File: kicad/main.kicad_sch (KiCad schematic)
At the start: 63 parts, among them J1 Jack-DC, J10 RS232, J11 UART, J2 LCD_Conn, J3 Data, J4 PWR, J5 uSD, J6 VIA_B, J7 IO~{EN}_{[2..7]}, J8 Control, J9 Addr, P1 Mini-DIN-6, SW1 Step, SW2 Reset, U1 74HC00, U2 74HC00, U3 MAX232, X1 4 MHz, X2 1.8432 MHz

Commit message: Add RTC & CR2032 battery, increase size of decoupling capacitors
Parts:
- removed J6: VIA_B, Connector_PinHeader_2.54mm:PinHeader_1x08_P2.54mm_Vertical, symbol Connector:Conn_01x08_Pin
- added BT1: CR2032, my:BatteryHolder_CR2032, symbol Device:Battery_Cell
- added J12: I2C1, Connector_PinHeader_2.54mm:PinHeader_1x04_P2.54mm_Horizontal, symbol Connector:Conn_01x04_Pin
- added J13: I2C2, Connector_PinHeader_2.54mm:PinHeader_2x02_P2.54mm_Vertical, symbol Connector:Conn_01x04_Pin
- added J6: VIA_B, Connector_PinHeader_2.54mm:PinHeader_1x04_P2.54mm_Vertical, symbol Connector:Conn_01x04_Pin
- added R10, R11: 5K, Resistor_THT:R_Axial_DIN0204_L3.6mm_D1.6mm_P7.62mm_Horizontal, symbol Device:R
- added U4: DS1307N+, Package_DIP:DIP-8_W7.62mm, symbol Timer_RTC:DS1307N+
- added U5: MCP9808_MSOP, Package_SO:MSOP-8_3x3mm_P0.65mm, symbol Sensor_Temperature:MCP9808_MSOP
- added Y1: 32.768 KHz, Crystal:Crystal_C26-LF_D2.1mm_L6.5mm_Horizontal, symbol Device:Crystal
- C11, C3, C4, C5, C7, C8: footprint Capacitor_THT:C_Disc_D3.0mm_W2.0mm_P2.50mm -> Capacitor_THT:C_Rect_L13.0mm_W3.0mm_P10.00mm_FKS3_FKP3_MKS4
- C16, C2, C6, C9: footprint Capacitor_THT:C_Disc_D3.0mm_W2.0mm_P2.50mm -> Capacitor_THT:C_Rect_L18.0mm_W5.0mm_P15.00mm_FKS3_FKP3
- R8, R9: footprint Resistor_THT:R_Axial_DIN0204_L3.6mm_D1.6mm_P2.54mm_Vertical -> Resistor_THT:R_Axial_DIN0204_L3.6mm_D1.6mm_P7.62mm_Horizontal
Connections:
- net +5V: now also J12.2 (Pin_2), J13.2 (Pin_2), J6.2 (Pin_2), R10.2, R11.2, U4.8 (VCC), U5.8 (V_{DD})
- net GND: now also BT1.2 (-), J12.1 (Pin_1), J13.1 (Pin_1), J6.1 (Pin_1), U4.4 (GND), U5.4 (GND), U5.5 (A2), U5.6 (A1), U5.7 (A0)
- net I^{2}CDATA: now reaches VIA1.15 (PB5)
- net I^{2}CDATA: now also J12.4 (Pin_4), J13.4 (Pin_4), R10.1, U4.5 (SDA), U5.1 (SDA)
- net I^{2}CCLK: now reaches VIA1.16 (PB6)
- net I^{2}CCLK: now also J12.3 (Pin_3), J13.3 (Pin_3), R11.1, U4.6 (SCL), U5.2 (SCL)
- net at VIA1.17 (PB7): now also J6.3 (Pin_3)
- net at VIA1.18 (CB1): now also J6.4 (Pin_4)
- new net: BT1.1 (+), U4.3 (VBAT)
- new net: U4.1 (X1), Y1.1
- new net: U4.2 (X2), Y1.2
- no-connect marks 21 -> 23
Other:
- note added: "8 256B blocks (C000-C7FF)"
- note added: "RTC"
- note added: "Temperature"
- note removed: "8 256-byte IO blocks (C000-C7FF)"
- moved on the sheet: C1, C11, C2, C3, C4, C5, C6, C7, C8, C9, CPU1, D1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

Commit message: WIP: V16
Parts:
- removed C11, C4: 0,1uF, Capacitor_THT:C_Rect_L13.0mm_W3.0mm_P10.00mm_FKS3_FKP3_MKS4, symbol Device:C
- removed C12, C13, C14, C15: 10uF, Capacitor_THT:CP_Radial_D5.0mm_P2.50mm, symbol Device:C_Polarized
- removed C5, C7: 0.1uF, Capacitor_THT:C_Rect_L13.0mm_W3.0mm_P10.00mm_FKS3_FKP3_MKS4, symbol Device:C
- removed J10: RS232, Connector_Dsub:DSUB-9_Male_Horizontal_P2.77x2.84mm_EdgePinOffset4.94mm_Housed_MountingHolesOffset7.48mm, symbol Connector:DE9_Plug
- removed J11: UART, Connector_PinHeader_2.54mm:PinHeader_1x04_P2.54mm_Horizontal, symbol Connector:Conn_01x04_Pin
- removed J13: I2C2, Connector_PinHeader_2.54mm:PinHeader_2x02_P2.54mm_Vertical, symbol Connector:Conn_01x04_Pin
- removed J2: LCD_Conn, my:LCD_4004, symbol Connector:Conn_01x18_Socket
- removed J7: IO~{EN}_{[2..7]}, Connector_PinHeader_2.54mm:PinHeader_1x06_P2.54mm_Vertical, symbol Connector:Conn_01x06_Pin
- removed JP1: Clock_Mode, Connector_PinHeader_2.54mm:PinHeader_1x03_P2.54mm_Vertical, symbol Jumper:Jumper_3_Open
- removed JP2: ACIA~{IRQ}, Connector_PinHeader_2.54mm:PinHeader_1x02_P2.54mm_Vertical, symbol Jumper:Jumper_2_Open
- removed JP3: ACIA~{NMI}, Connector_PinHeader_2.54mm:PinHeader_1x02_P2.54mm_Vertical, symbol Jumper:Jumper_2_Open
- removed JP4: VIA~{IRQ}, Connector_PinHeader_2.54mm:PinHeader_1x02_P2.54mm_Vertical, symbol Jumper:Jumper_2_Open
- removed JP5: VIA~{NMI}, Connector_PinHeader_2.54mm:PinHeader_1x02_P2.54mm_Vertical, symbol Jumper:Jumper_2_Open
- removed JP6: ~{CTS}, Connector_PinHeader_2.54mm:PinHeader_1x02_P2.54mm_Vertical, symbol Jumper:Jumper_2_Open
- removed STEP1: DS1813, Package_TO_SOT_THT:TO-92, symbol ds1813:DS1813-5+
- removed SW1: Step, Button_Switch_THT:SW_PUSH_6mm_H5mm, symbol Switch:SW_Push
- removed U3: MAX232, Package_DIP:DIP-16_W7.62mm_Socket, symbol Interface_UART:MAX232
- added C10: 10uF, Capacitor_THT:C_Disc_D3.0mm_W2.0mm_P2.50mm, symbol Device:C
- added C12: 22uF, Capacitor_THT:C_Disc_D3.0mm_W2.0mm_P2.50mm, symbol Device:C
- added C13: 0.1uF, Capacitor_THT:C_Rect_L18.0mm_W5.0mm_P15.00mm_FKS3_FKP3, symbol Device:C
- added D3: DATA, LED_THT:LED_D3.0mm, symbol Device:LED
- added J14: LCD_Conn, my:LCD24064, symbol Connector:Conn_01x22_Socket
- added J15: VIA_A, Connector_PinHeader_2.54mm:PinHeader_2x06_P2.54mm_Vertical, symbol Connector:Conn_01x12_Pin
- added J2: UART, Connector_PinHeader_2.54mm:PinHeader_1x04_P2.54mm_Horizontal, symbol Connector:Conn_01x04_Pin
- added J7: IO~{EN}_{[3..7]}, Connector_PinHeader_2.54mm:PinHeader_1x05_P2.54mm_Vertical, symbol Connector:Conn_01x05_Pin
- added MH3: MountingHole, my:Hole_3.5x5, symbol Custom_Symbols_Library:MountingHole
- added R12: 300, Resistor_THT:R_Axial_DIN0204_L3.6mm_D1.6mm_P7.62mm_Horizontal, symbol Device:R
- added R13, R14, R15: 10K, Resistor_THT:R_Axial_DIN0204_L3.6mm_D1.6mm_P7.62mm_Horizontal, symbol Device:R
- added SW3: SW_PWR, my:PB22E06, symbol Switch:SW_DPST
- added U3: AMS1117, Package_TO_SOT_SMD:SOT-223-3_TabPin2, symbol Regulator_Linear:AMS1117
- added U6: GAL16V8, Package_DIP:DIP-20_W7.62mm_Socket, symbol Logic_Programmable:GAL16V8
- added U7: ESP-01, my:ESP-01, symbol my:ESP-01
- J12: footprint Connector_PinHeader_2.54mm:PinHeader_1x04_P2.54mm_Horizontal -> Connector_PinHeader_2.54mm:PinHeader_2x02_P2.54mm_Vertical
- R8, R9: footprint Resistor_THT:R_Axial_DIN0204_L3.6mm_D1.6mm_P7.62mm_Horizontal -> Resistor_THT:R_Axial_DIN0204_L3.6mm_D1.6mm_P2.54mm_Vertical
- X1: value 4 MHz -> 16 MHz
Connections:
- net +5V: now also RV1.1, C10.1, C13.1, J14.19 (Pin_19), J14.21 (Pin_21), J14.3 (Pin_3), J15.2 (Pin_2), J2.2 (Pin_2), U3.3 (VI), U6.20 (VCC); no longer RV1.3
- net +9V: now also SW3.4; no longer J1.1
- net A_{0}: now also J14.8 (Pin_8)
- net D_{0}: now also J14.11 (Pin_11)
- net D_{1}: now also J14.12 (Pin_12)
- net D_{2}: now also J14.13 (Pin_13)
- net D_{3}: now also J14.14 (Pin_14)
- net D_{4}: now also J14.15 (Pin_15)
- net D_{5}: now also J14.16 (Pin_16)
- net D_{6}: now also J14.17 (Pin_17)
- net D_{7}: now also J14.18 (Pin_18)
- net GND: now also ACIA1.9 (~{CTS}), C10.2, C12.2, C13.2, D3.1 (K), J14.2 (Pin_2), J14.22 (Pin_22), J15.1 (Pin_1), J2.1 (Pin_1), SW3.2, U3.1 (ADJ), U6.10 (GND), U6.11 (I10/~{OE}), U7.4 (GND); no longer J1.2, RV1.1
- net IO~{EN}_{3}: now also J7.1 (Pin_1)
- net IO~{EN}_{4}: now also J7.2 (Pin_2)
- net IO~{EN}_{5}: now also J7.3 (Pin_3)
- net IO~{EN}_{6}: now also J7.4 (Pin_4)
- net IO~{EN}_{7}: now also J7.5 (Pin_5)
- net ~{IRQ}: now also ACIA1.26 (~{IRQ}), VIA1.21 (~{IRQ})
- net ~{RD}: now also J14.6 (Pin_6)
- net ~{WD}: now also J14.5 (Pin_5)
- net Ф2: now also U6.13 (IO7); no longer CPU1.37 (ϕ0)
- net TX: now reaches ACIA1.10 (TxD)
- net TX: now also J2.3 (Pin_3), U7.1 (RX)
- net RX: now reaches ACIA1.12 (RxD)
- net RX: now also J2.4 (Pin_4), U7.5 (TX)
- net at RV1.2: now also J14.4 (Pin_4)
- net at VIA1.39 (CA2): now also J15.12 (Pin_12)
- net at VIA1.40 (CA1): now also J15.11 (Pin_11)
- net CLK: no longer names the net of X1.8 (OUT)
- net CLK: now also U6.1 (I1/CLK)
- net IO~{EN}_{2} renamed LCD~{EN}
- net LCD~{EN}: now also J14.7 (Pin_7), U6.2 (I2)
- net LCDD4: no longer names the net of VIA1.2 (PA0)
- net LCDD4: now also J15.3 (Pin_3)
- net LCDD5: no longer names the net of VIA1.3 (PA1)
- net LCDD5: now also J15.4 (Pin_4)
- net LCDD6: no longer names the net of VIA1.4 (PA2)
- net LCDD6: now also J15.5 (Pin_5)
- net LCDD7: no longer names the net of VIA1.5 (PA3)
- net LCDD7: now also J15.6 (Pin_6)
- net LCDEN1: no longer names the net of VIA1.6 (PA4)
- net LCDEN1: now also J15.7 (Pin_7)
- net LCDEN2: no longer names the net of VIA1.7 (PA5)
- net LCDEN2: now also J15.8 (Pin_8)
- net LCDRS: no longer names the net of VIA1.9 (PA7)
- net LCDRS: now also J15.10 (Pin_10)
- net LCDR~{W}: no longer names the net of VIA1.8 (PA6)
- net LCDR~{W}: now also J15.9 (Pin_9)
- new net: J1.1, SW3.3
- new net: J1.2, SW3.1
- new net: R14.1, U7.7 (~{RST})
- new net: D3.2 (A), R12.1
- new net: J14.20 (Pin_20), RV1.3
- new net: R13.1, U7.2 (GPIO0)
- new net: R12.2, U7.3 (GPIO2)
- new net: R15.1, U7.6 (CH_EN)
- new net +3.3V: C12.1, R13.2, R14.2, R15.2, U3.2 (VO), U7.8 (VCC)
- new net PHV: CPU1.37 (ϕ0), U6.12 (IO8)
- no-connect marks 23 -> 33
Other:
- note added: "$D200-$D2FF"
- note added: "24064 LCD Connector"
- note added: "Modem"
- note removed: "40x04 LCD Connector"
- moved on the sheet: ACIA1, BT1, C1, C16, C2, C3, C6, C8, C9, CPU1, D1, D2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

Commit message: WIP: V16 GAL stuff
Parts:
- removed J6: VIA_B, Connector_PinHeader_2.54mm:PinHeader_1x04_P2.54mm_Vertical, symbol Connector:Conn_01x04_Pin
- removed J7: IO~{EN}_{[3..7]}, Connector_PinHeader_2.54mm:PinHeader_1x05_P2.54mm_Vertical, symbol Connector:Conn_01x05_Pin
- added J7: IO~{EN}_{[3..4]}, Connector_PinHeader_2.54mm:PinHeader_1x02_P2.54mm_Vertical, symbol Connector:Conn_01x02_Pin
- J2: footprint Connector_PinHeader_2.54mm:PinHeader_1x04_P2.54mm_Horizontal -> Connector_PinHeader_2.54mm:PinHeader_1x04_P2.54mm_Vertical
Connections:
- net IO~{EN}_{3}: now also J7.1 (Pin_1)
- net IO~{EN}_{4}: now also J7.2 (Pin_2)
- net ~{RES}: now also U6.9 (I9)
- net IO~{EN}_{5}: no longer names the net of IO1.10 (O5)
- net IO~{EN}_{6}: no longer names the net of IO1.9 (O6)
- net IO~{EN}_{7}: no longer names the net of IO1.7 (O7)
- no-connect marks 33 -> 37
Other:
- moved on the sheet: X1

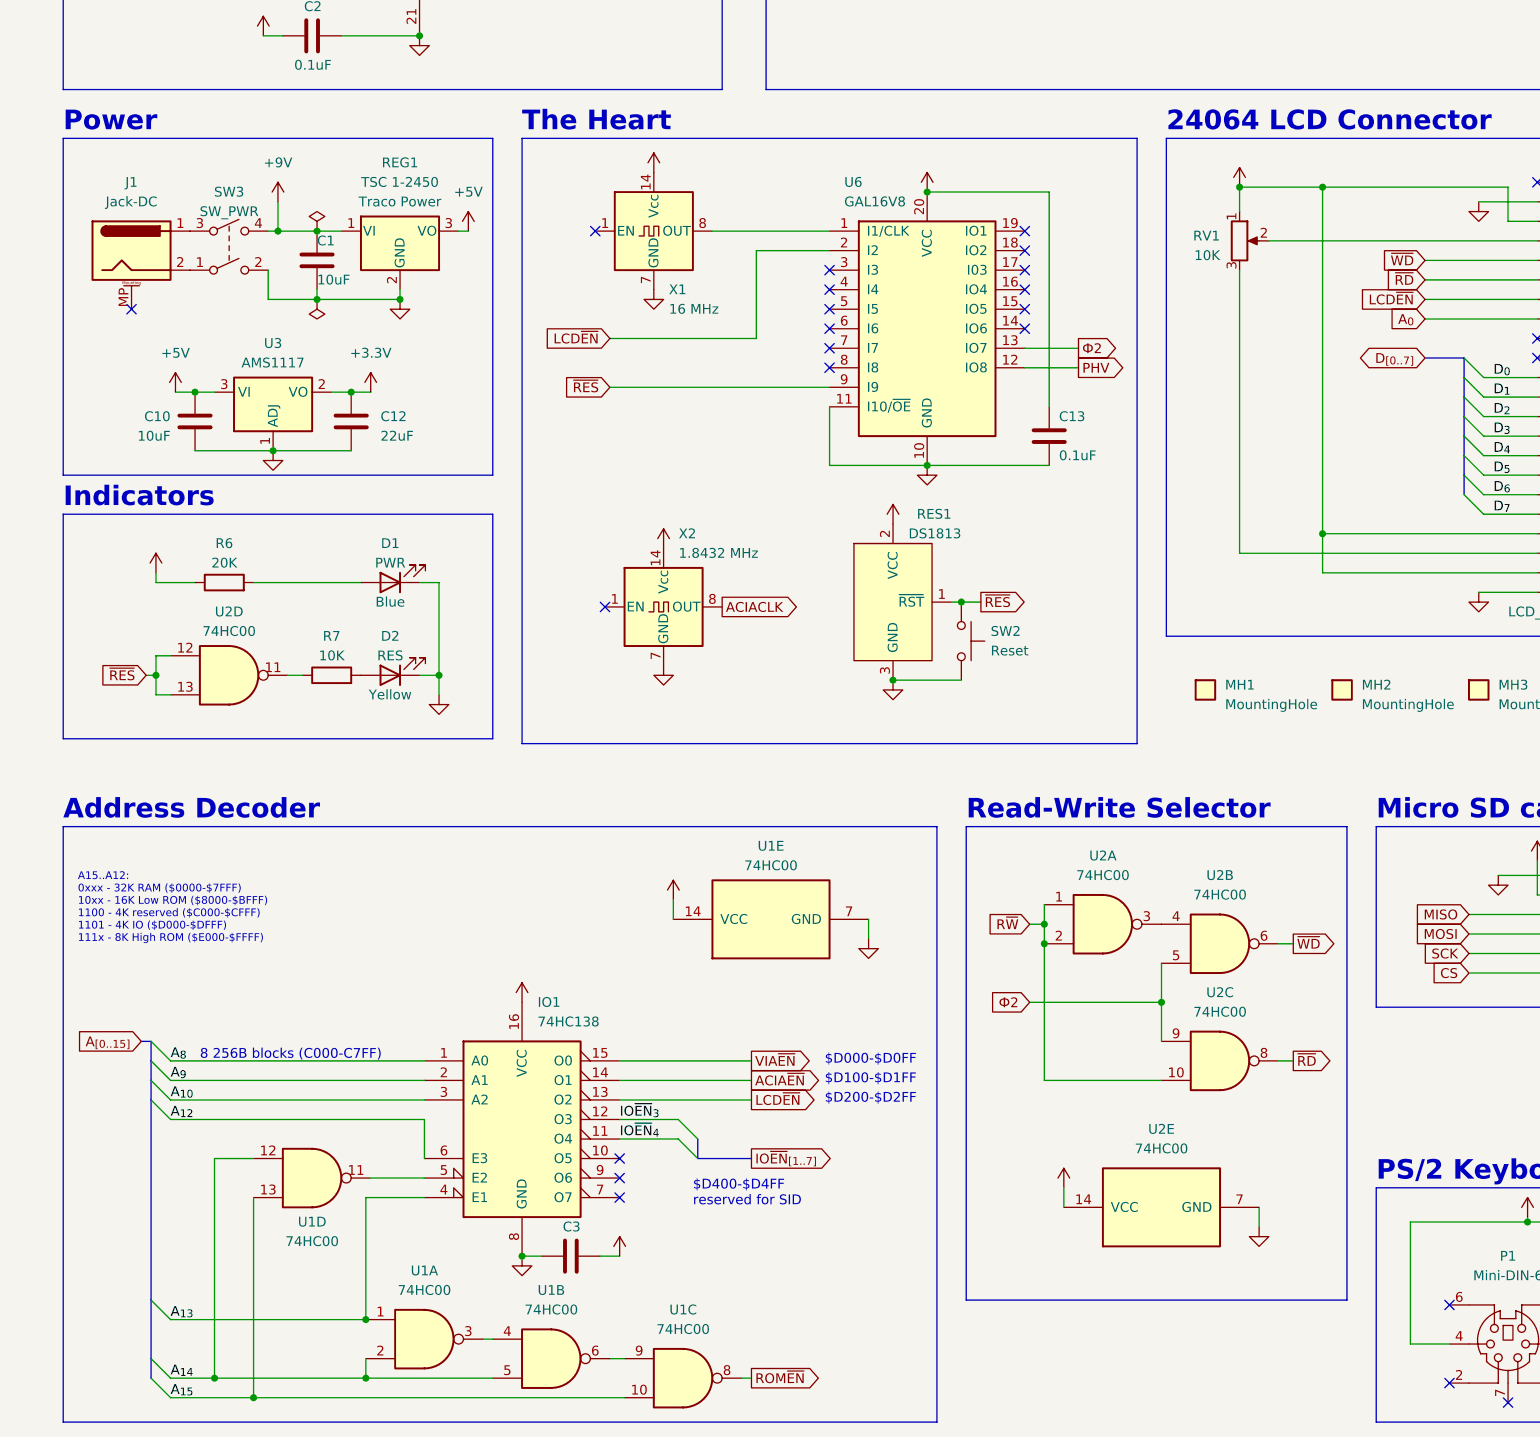
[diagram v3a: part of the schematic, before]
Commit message: Replace address decoder & r/w qualifier with GAL
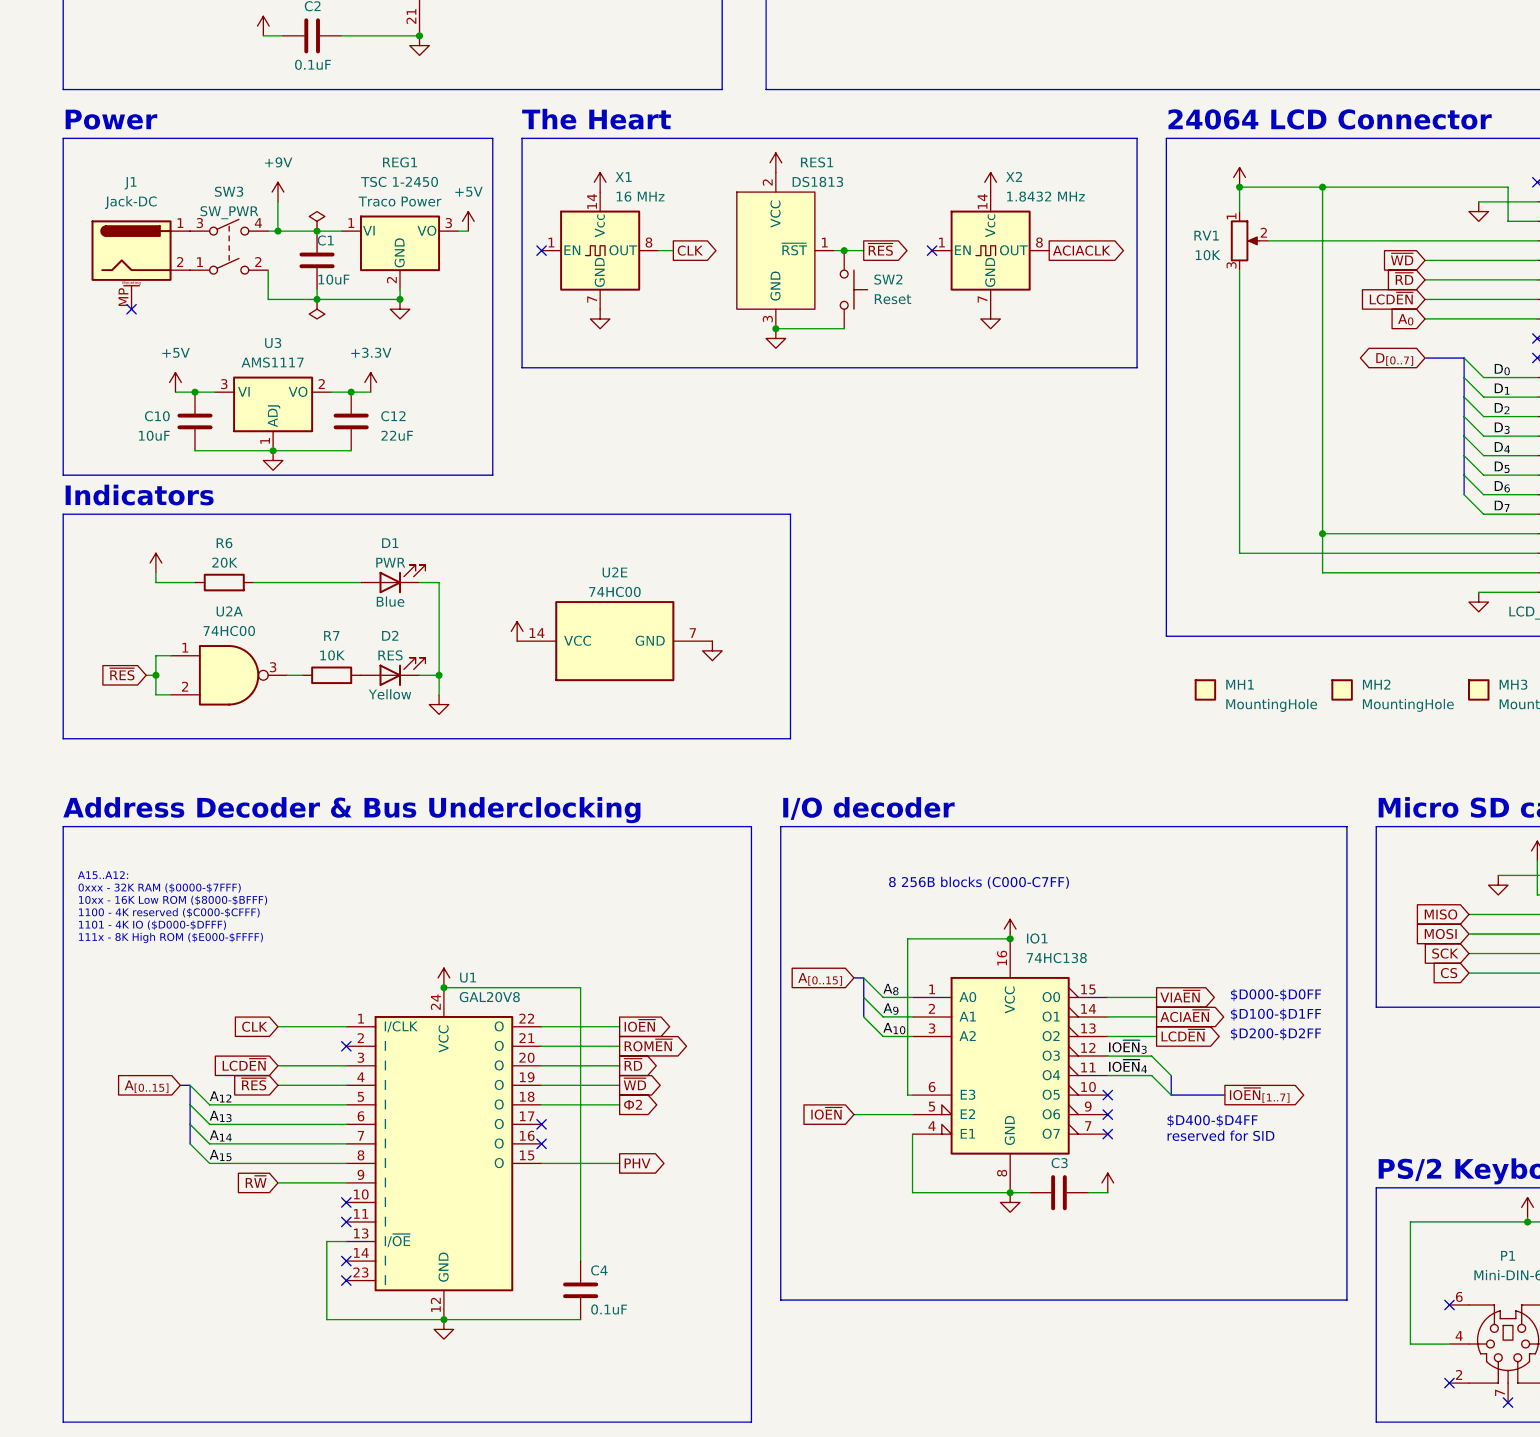
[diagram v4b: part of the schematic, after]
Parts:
- removed C13: 0.1uF, Capacitor_THT:C_Rect_L18.0mm_W5.0mm_P15.00mm_FKS3_FKP3, symbol Device:C
- removed U1: 74HC00, Package_DIP:DIP-14_W7.62mm_Socket, symbol 74xx:74HC00
- removed unit 1 of U2
- removed unit 3 of U2
- removed unit 2 of U2
- removed U6: GAL16V8, Package_DIP:DIP-20_W7.62mm_Socket, symbol Logic_Programmable:GAL16V8
- added C4: 0.1uF, Capacitor_THT:C_Rect_L18.0mm_W5.0mm_P15.00mm_FKS3_FKP3, symbol Device:C
- added U1: GAL20V8, Package_DIP:DIP-24_W7.62mm_Socket, symbol my:GAL20V8
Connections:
- net +5V: now also IO1.6 (E3), C4.1, U1.24 (VCC)
- net A_{12}: now also U1.5 (I); no longer IO1.6 (E3)
- net A_{13}: now also U1.6 (I); no longer IO1.4 (E1)
- net A_{14}: now also U1.7 (I)
- net A_{15}: now also U1.8 (I)
- net GND: now also IO1.4 (E1), C4.2, U1.12 (GND), U1.13 (I/~{OE})
- net LCD~{EN}: now also U1.3 (I)
- net PHV: now also U1.15 (O)
- net ROM~{EN}: now also U1.21 (O)
- net R~{W}: now also U1.9 (I)
- net ~{RD}: now also U1.20 (O)
- net ~{RES}: now also U2.1, U2.2, U1.4 (I); no longer U2.12, U2.13
- net ~{WD}: now also U1.19 (O)
- net Ф2: now also U1.18 (O)
- net CLK: now reaches X1.8 (OUT)
- net CLK: now also U1.1 (I/CLK)
- net at R7.1: now also U2.3; no longer U2.11
- net IO~{EN}: now reaches IO1.5 (E2)
- net IO~{EN}: now also U1.22 (O)
- no-connect marks 37 -> 32
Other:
- note added: "Address Decoder & Bus Underclocking"
- note added: "I/O decoder"
- note removed: "Address Decoder"
- note removed: "Read-Write Selector"
- moved on the sheet: C3, IO1, RES1, SW2, X1, X2
